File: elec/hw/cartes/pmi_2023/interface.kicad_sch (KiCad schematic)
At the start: 35 parts, among them SW3 MSS12C02LS-BB2.0, SW4 2425755-1, SW5 DS1040-04RN, U11 XRA1200PIG16TR-F, U18 EESX1321

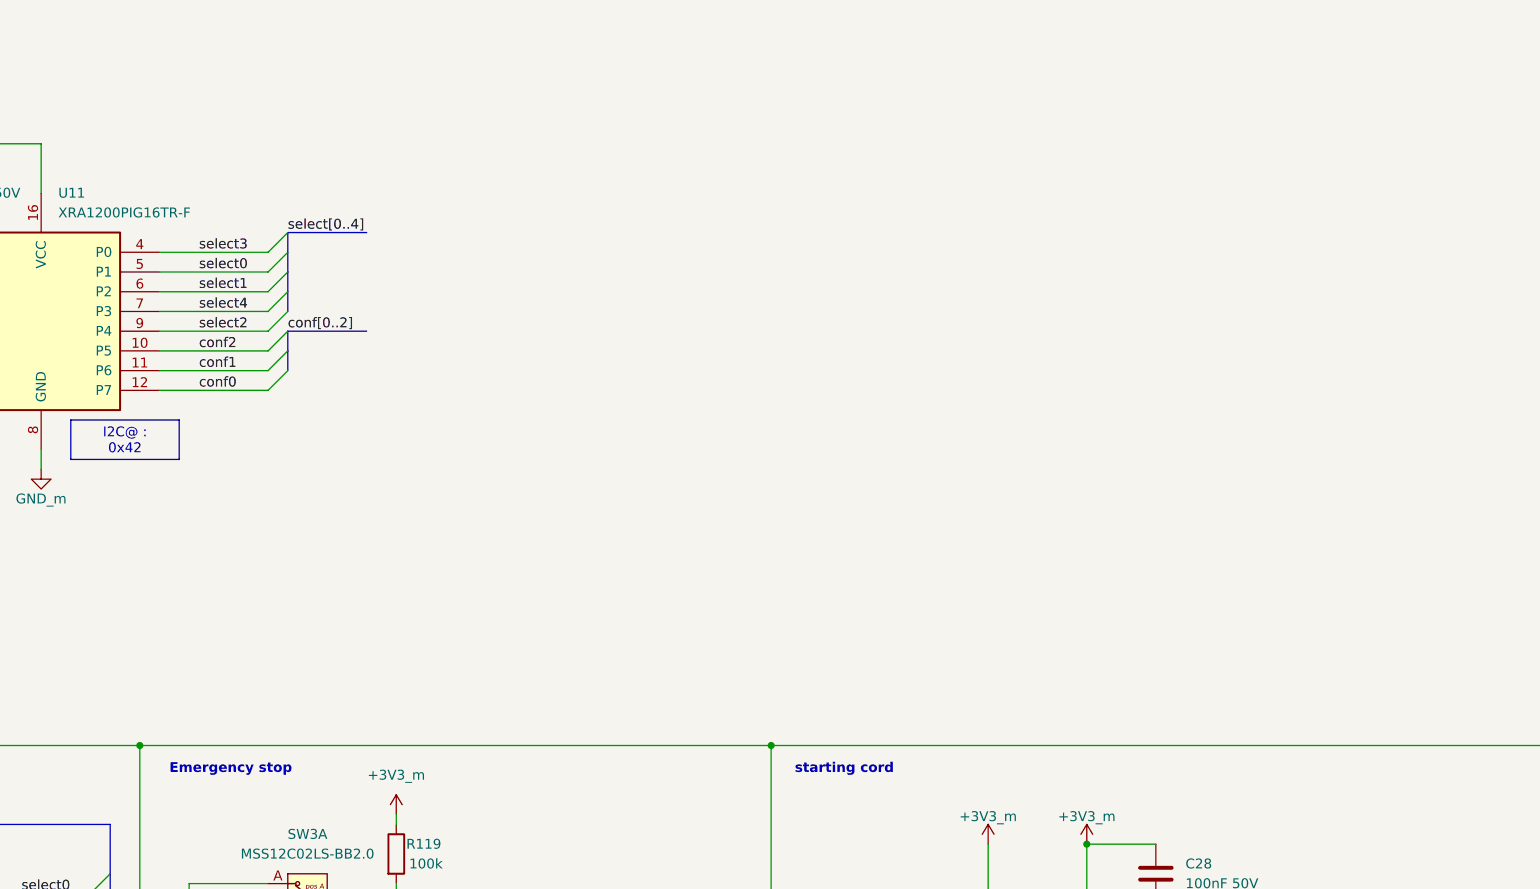
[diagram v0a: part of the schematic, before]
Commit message: pmi_tof_sensor : last commit before tmf8821 deletion
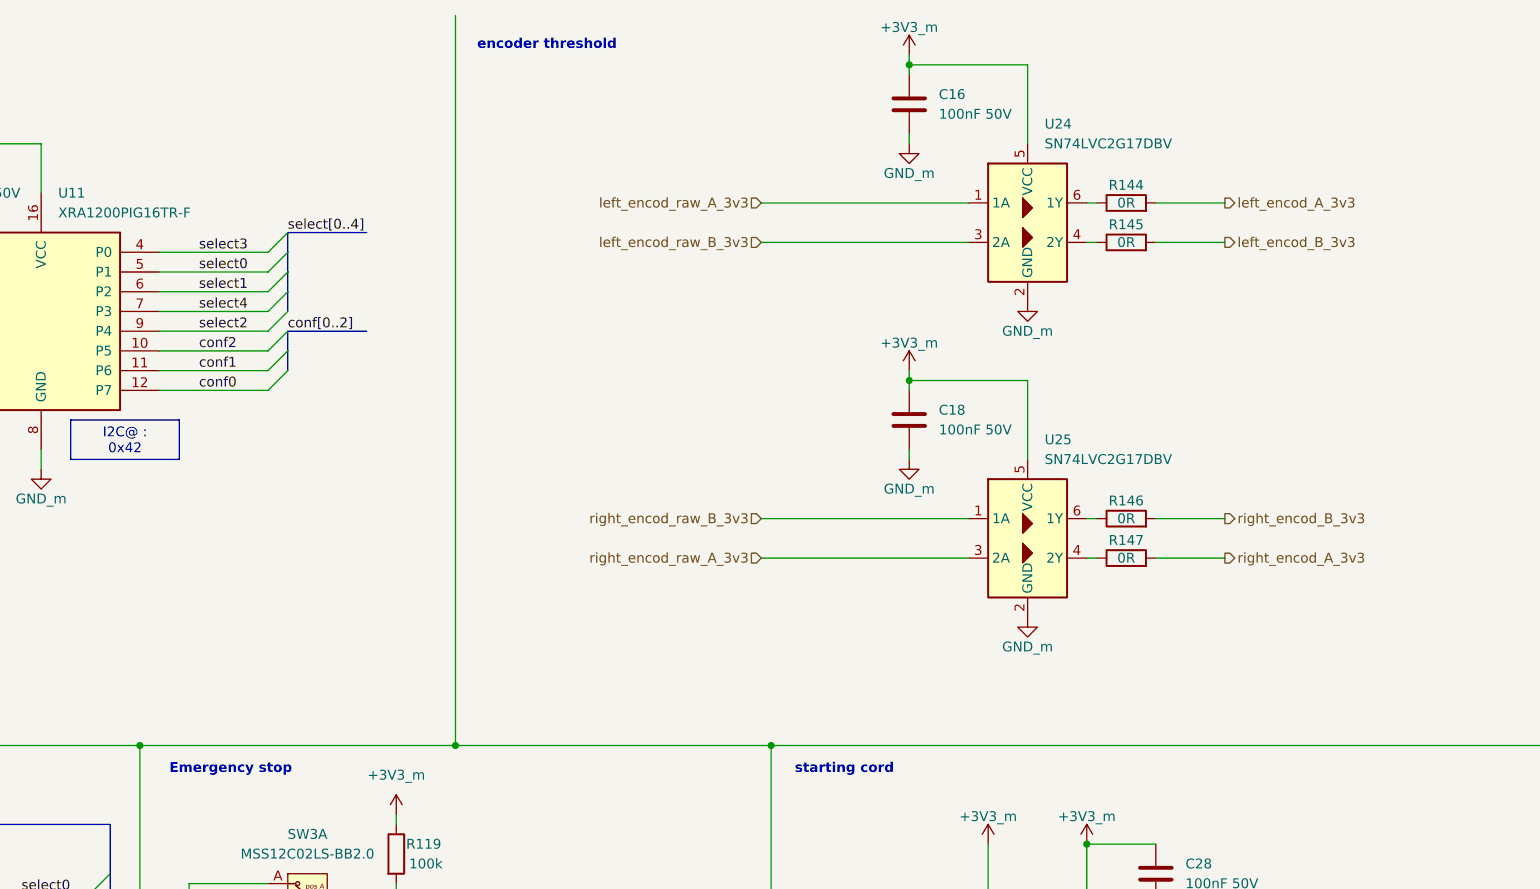
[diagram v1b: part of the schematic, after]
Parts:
- added C16, C18: 100nF 50V, cocotter_capacitors:C_0603_1608Metric, symbol cocotter_capacitors:C_100nF_50V_0603
- added R144, R145, R146, R147: 0R, cocotter_resistor:r0603_reflow, symbol cocotter_resistors:R_0R_0603
- added U24, U25: SN74LVC2G17DBV, cocotter_ic:SOT-23-6, symbol cocotter_ic:SN74LVC2G17DBV
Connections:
- net +3V3_m: now also C16.1, C18.1, U24.5 (VCC), U25.5 (VCC)
- net GND_m: now also C16.2, C18.2, U24.2 (GND), U25.2 (GND)
- new net: R145.1, U24.4 (2Y)
- new net: R144.1, U24.6 (1Y)
- new net: R147.1, U25.4 (2Y)
- new net: R146.1, U25.6 (1Y)
- new net left_encod_A_3v3: R144.2
- new net left_encod_B_3v3: R145.2
- new net left_encod_raw_A_3v3: U24.1 (1A)
- new net left_encod_raw_B_3v3: U24.3 (2A)
- new net right_encod_A_3v3: R147.2
- new net right_encod_B_3v3: R146.2
- new net right_encod_raw_A_3v3: U25.3 (2A)
- new net right_encod_raw_B_3v3: U25.1 (1A)
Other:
- note added: "encoder threshold"

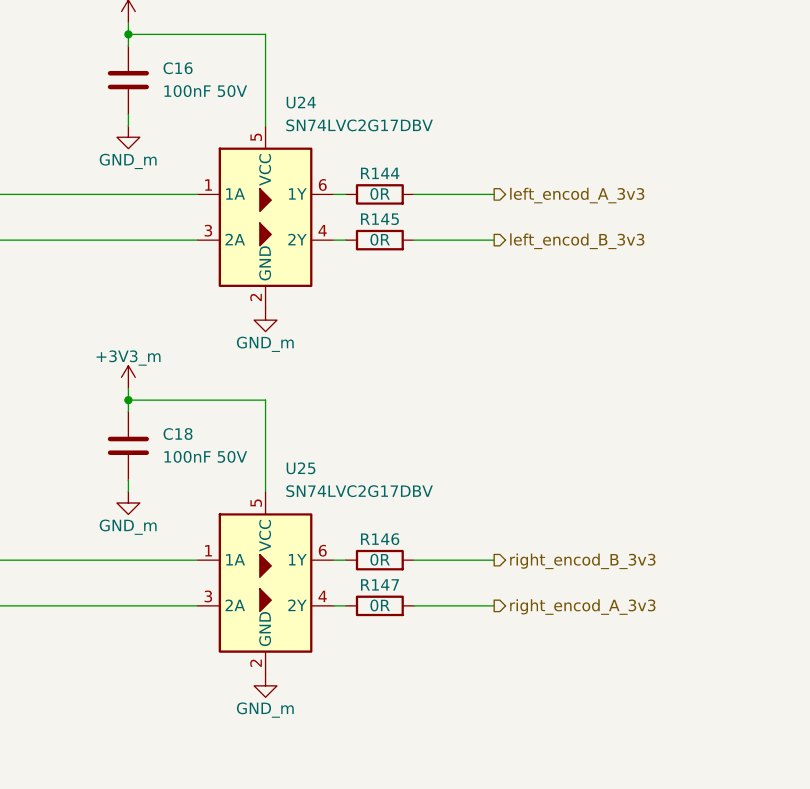
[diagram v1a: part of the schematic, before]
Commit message: modified mounting hole, replaced transistors to place them in bottom layer
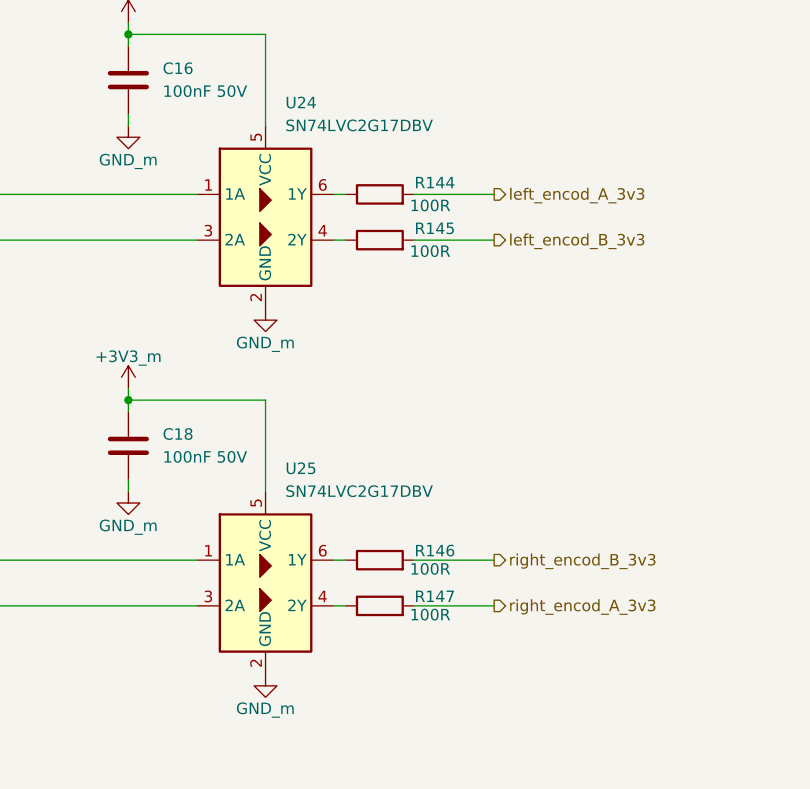
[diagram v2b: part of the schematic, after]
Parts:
- R144, R145, R146, R147: value 0R -> 100R; symbol cocotter_resistors:R_0R_0603 -> cocotter_resistors:R_100R_0603_1%; JLCPCB C431718 -> C22775; Specification 0R 0603 20mOhms max 100mW -> 100R 0603 1% 100mW
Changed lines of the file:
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@@
 	)
 	(symbol
-		(lib_id "cocotter_resistors:R_0R_0603")
+		(lib_id "cocotter_resistors:R_100R_0603_1%")
 		(at 222.25 82.55 90)
 		(unit 1)
@@
 		(dnp no)
 		(property "Reference" "R147"
-			(at 222.25 80.264 90)
-			(effects
-				(font
-					(size 1.27 1.27)
-				)
-			)
-		)
-		(property "Value" "0R"
-			(at 222.25 82.55 90)
+			(at 230.632 81.534 90)
+			(effects
+				(font
+					(size 1.27 1.27)
+				)
+				(justify left)
+			)
+		)
+		(property "Value" "100R"
+			(at 227.838 83.566 90)
 			(effects
 				(font
@@
 			)
 		)
-		(property "Specification" "0R 0603 20mOhms max 100mW"
+		(property "Specification" "100R 0603 1% 100mW"
 			(at 222.25 82.55 0)
 			(effects
@@
 			)
 		)
-		(property "JLCPCB" "C431718"
+		(property "JLCPCB" "C22775"
 			(at 222.25 82.55 0)
 			(effects
@@
 	)
 	(symbol
-		(lib_id "cocotter_resistors:R_0R_0603")
+		(lib_id "cocotter_resistors:R_100R_0603_1%")
 		(at 222.25 36.83 90)
 		(unit 1)
@@
 		(dnp no)
 		(property "Reference" "R144"
-			(at 222.25 34.544 90)
-			(effects
-				(font
-					(size 1.27 1.27)
-				)
-			)
-		)
-		(property "Value" "0R"
-			(at 222.25 36.83 90)
+			(at 230.632 35.56 90)
+			(effects
+				(font
+					(size 1.27 1.27)
+				)
+				(justify left)
+			)
+		)
+		(property "Value" "100R"
+			(at 227.838 38.1 90)
 			(effects
 				(font
@@
 			)
 		)
-		(property "Specification" "0R 0603 20mOhms max 100mW"
+		(property "Specification" "100R 0603 1% 100mW"
 			(at 222.25 36.83 0)
 			(effects
@@
 			)
 		)
-		(property "JLCPCB" "C431718"
+		(property "JLCPCB" "C22775"
 			(at 222.25 36.83 0)
 			(effects
@@
 	)
 	(symbol
-		(lib_id "cocotter_resistors:R_0R_0603")
+		(lib_id "cocotter_resistors:R_100R_0603_1%")
 		(at 222.25 77.47 90)
 		(unit 1)
@@
 		(dnp no)
 		(property "Reference" "R146"
-			(at 222.25 75.184 90)
-			(effects
-				(font
-					(size 1.27 1.27)
-				)
-			)
-		)
-		(property "Value" "0R"
-			(at 222.25 77.47 90)
+			(at 230.632 76.454 90)
+			(effects
+				(font
+					(size 1.27 1.27)
+				)
+				(justify left)
+			)
+		)
+		(property "Value" "100R"
+			(at 227.838 78.486 90)
 			(effects
 				(font
@@
 			)
 		)
-		(property "Specification" "0R 0603 20mOhms max 100mW"
+		(property "Specification" "100R 0603 1% 100mW"
 			(at 222.25 77.47 0)
 			(effects
@@
 			)
 		)
-		(property "JLCPCB" "C431718"
+		(property "JLCPCB" "C22775"
 			(at 222.25 77.47 0)
 			(effects
@@
 	)
 	(symbol
-		(lib_id "cocotter_resistors:R_0R_0603")
+		(lib_id "cocotter_resistors:R_100R_0603_1%")
 		(at 222.25 41.91 90)
 		(unit 1)
@@
 		(dnp no)
 		(property "Reference" "R145"
-			(at 222.25 39.624 90)
-			(effects
-				(font
-					(size 1.27 1.27)
-				)
-			)
-		)
-		(property "Value" "0R"
-			(at 222.25 41.91 90)
+			(at 230.632 40.64 90)
+			(effects
+				(font
+					(size 1.27 1.27)
+				)
+				(justify left)
+			)
+		)
+		(property "Value" "100R"
+			(at 227.838 43.18 90)
 			(effects
 				(font
@@
 			)
 		)
-		(property "Specification" "0R 0603 20mOhms max 100mW"
+		(property "Specification" "100R 0603 1% 100mW"
 			(at 222.25 41.91 0)
 			(effects
@@
 			)
 		)
-		(property "JLCPCB" "C431718"
+		(property "JLCPCB" "C22775"
 			(at 222.25 41.91 0)
 			(effects

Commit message: BAU moved to bottom layer
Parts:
- R102: now not fitted
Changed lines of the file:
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@@
 		(in_bom yes)
 		(on_board yes)
-		(dnp no)
+		(dnp yes)
 		(fields_autoplaced yes)
 		(property "Reference" "R102"

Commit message: start sensor replaced
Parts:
- removed R121: 1k 1%, cocotter_resistor:r0603_reflow, symbol cocotter_resistors:R_1k_0603_1%
- R120: value 1k 1% -> 390R 1%; symbol cocotter_resistors:R_1k_0603_1% -> cocotter_resistors:R_390R_0603_1%; JLCPCB C21190 -> C23151; Specification 10k 0603 1% 100mW -> 390R 0603 1% 100mW
- R122: value 100k -> 10k 1%; symbol cocotter_resistors:R_100k_0603_1% -> cocotter_resistors:R_10k_0603_1%; JLCPCB C25803 -> C25804; Specification 100k 0603 1% 100mW -> 10k 0603 1% 100mW
- U18: value EESX1321 -> RPI-222N1; footprint cocotter_ic:EESX1321 -> cocotter_ic:RPI-222; symbol cocotter_ic:EESX1321 -> cocotter_ic:RPI-222N1; JLCPCB (none) -> C403662
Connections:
- net +3V3_m: now also U18.2 (A), U18.3 (C); no longer U18.1 (A), U18.6 (C)
- net start_robot_3v3: now also U18.4 (E); no longer U18.5 (E2)
- net at R120.1: now also U18.1 (C); no longer U18.2 (C1)
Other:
- moved on the sheet: C28, R120

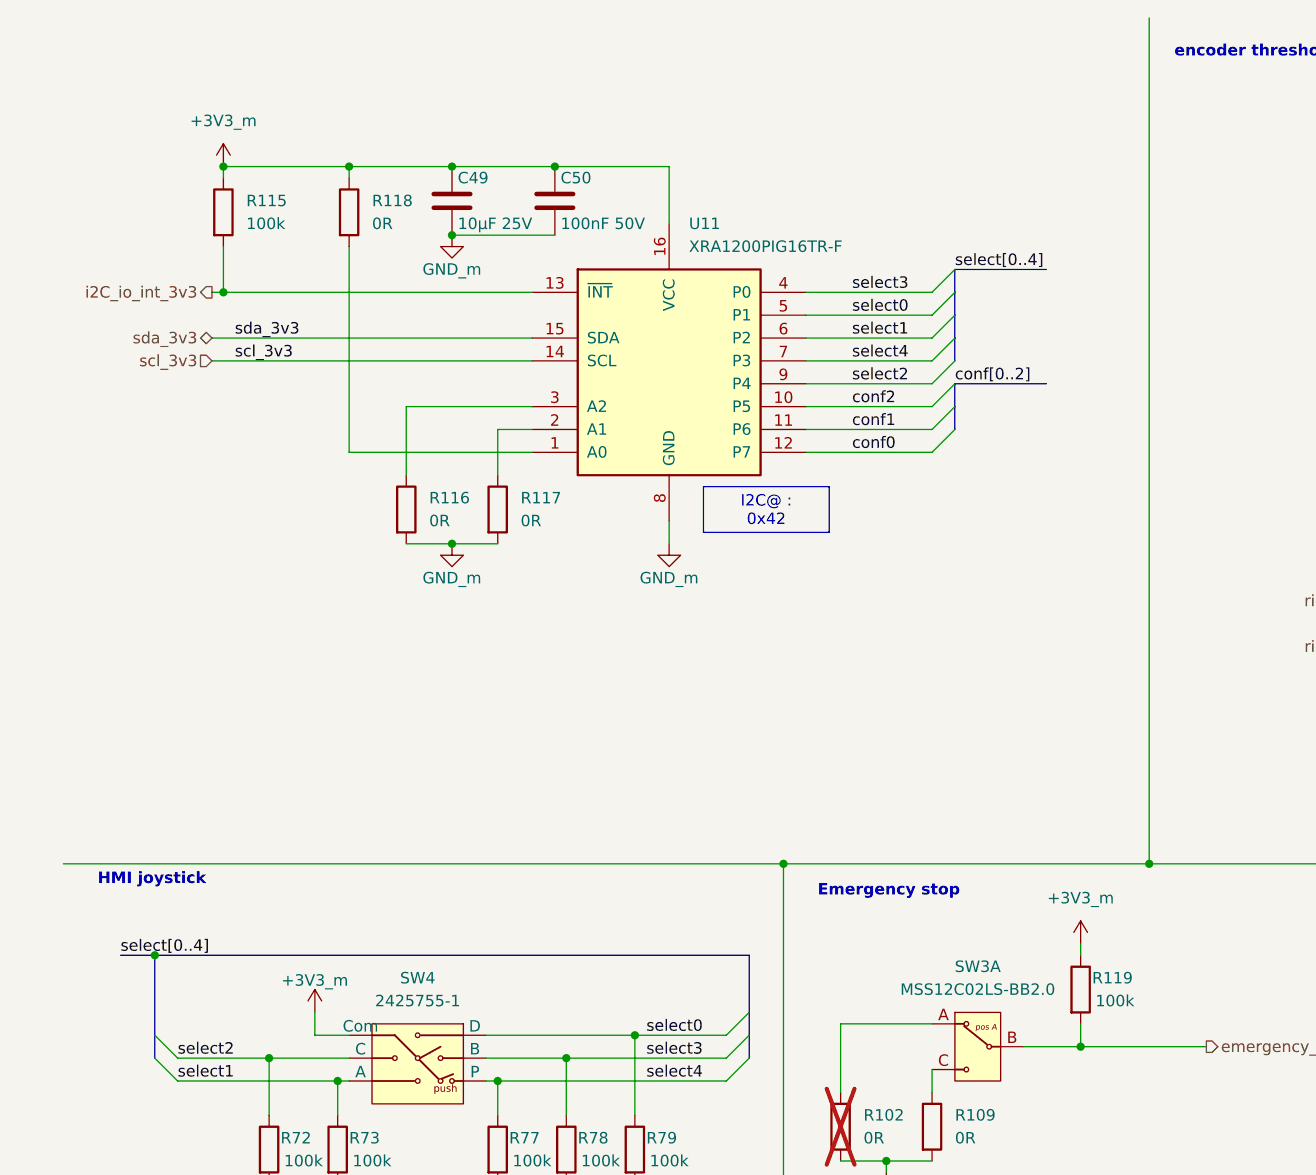
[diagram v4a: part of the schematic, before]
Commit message: XRA1200 replaced by TCA6408
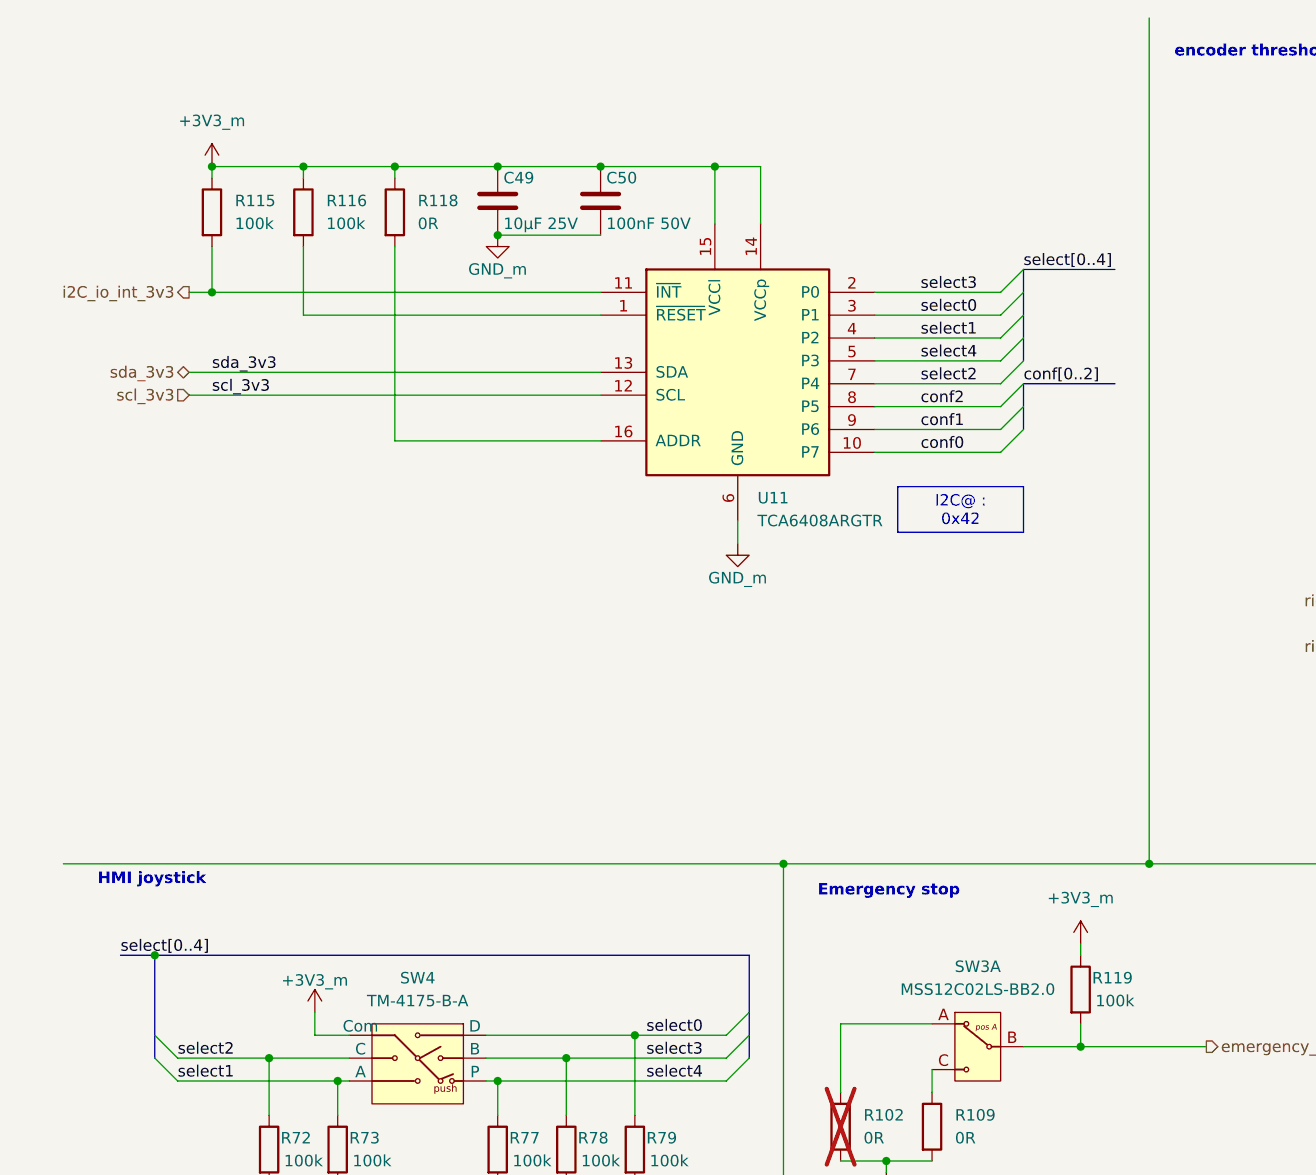
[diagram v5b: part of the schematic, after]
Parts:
- removed R117: 0R, cocotter_resistor:r0603_reflow, symbol cocotter_resistors:R_0R_0603
- C16, C18, C28, C31, C50: JLCPCB C14663 -> (none); JLCPCB Part # (none) -> C14663
- C49: JLCPCB C15850 -> (none); JLCPCB Part # (none) -> C15850
- R102, R109, R118, R132, R133, R134, R135: JLCPCB C431718 -> (none); JLCPCB Part # (none) -> C431718
- R115, R119, R68, R69, R70, R71, R72, R73, R77, R78, R79: JLCPCB C25803 -> (none); JLCPCB Part # (none) -> C25803
- R116: value 0R -> 100k; symbol cocotter_resistors:R_0R_0603 -> cocotter_resistors:R_100k_0603_1%; JLCPCB C431718 -> (none); JLCPCB Part # (none) -> C25803; Specification 0R 0603 20mOhms max 100mW -> 100k 0603 1% 100mW; mouser (none) -> 603-RC0603FR-10100KL
- R120: JLCPCB C23151 -> (none); JLCPCB Part # (none) -> C23151
- R122: JLCPCB C25804 -> (none); JLCPCB Part # (none) -> C25804
- R144, R145, R146, R147: JLCPCB C22775 -> (none); JLCPCB Part # (none) -> C22775
- R80, R81: JLCPCB C2991540 -> (none); JLCPCB Part # (none) -> C2991540
- SW3: JLCPCB C3008585 -> (none); JLCPCB Part # (none) -> C3008585
- SW4: value 2425755-1 -> TM-4175-B-A; JLCPCB C465995 -> (none); JLCPCB Part # (none) -> C465995
- SW5: JLCPCB C3024970 -> (none); JLCPCB Part # (none) -> C3024970
- U11: value XRA1200PIG16TR-F -> TCA6408ARGTR; footprint cocotter_ic:TSSOP-16_4.4x5mm_P0.65mm -> cocotter_ic:VQFN-16-1EP_3x3mm_P0.5mm_EP1.1x1.1mm; symbol cocotter_ic:XRA1200PIG16TR-F -> cocotter_ic:TCA6408ARGTR; JLCPCB C2669711 -> (none); JLCPCB part# (none) -> C181499; mouser 701-XRA1200PIG16TR-F -> 595-TCA6408ARGTR
- U18: JLCPCB C403662 -> (none); JLCPCB Part # (none) -> C403662
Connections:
- net +3V3_m: now also R116.1, U11.14 (VCCp), U11.15 (VCCl); no longer U11.16 (VCC)
- net GND_m: now also U11.6 (GND); no longer R116.2, U11.8 (GND)
- net conf0: now also U11.10 (P7); no longer U11.12 (P7)
- net conf1: now also U11.9 (P6); no longer U11.11 (P6)
- net conf2: now also U11.8 (P5); no longer U11.10 (P5)
- net i2C_io_int_3v3: now also U11.11 (~{INT}); no longer U11.13 (~{INT})
- net scl_3v3: now also U11.12 (SCL); no longer U11.14 (SCL)
- net sda_3v3: now also U11.13 (SDA); no longer U11.15 (SDA)
- net select0: now also U11.3 (P1); no longer U11.5 (P1)
- net select1: now also U11.4 (P2); no longer U11.6 (P2)
- net select2: now also U11.7 (P4); no longer U11.9 (P4)
- net select3: now also U11.2 (P0); no longer U11.4 (P0)
- net select4: now also U11.5 (P3); no longer U11.7 (P3)
- net at U11.1 (~{RESET}): now also R116.2; no longer R118.2
- new net: R118.2, U11.16 (ADDR)
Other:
- moved on the sheet: C49, C50, R115, R116, R118, U11
